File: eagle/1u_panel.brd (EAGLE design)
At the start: 83 x 100 mm, 61 parts, among them J1 1.27MM-SWD-CONNECTOR, U1 SPV1040, U5 P-CHANNELFET, U6 ON-N-CHANNEL-FET, U7 DIODE-INC-NPN

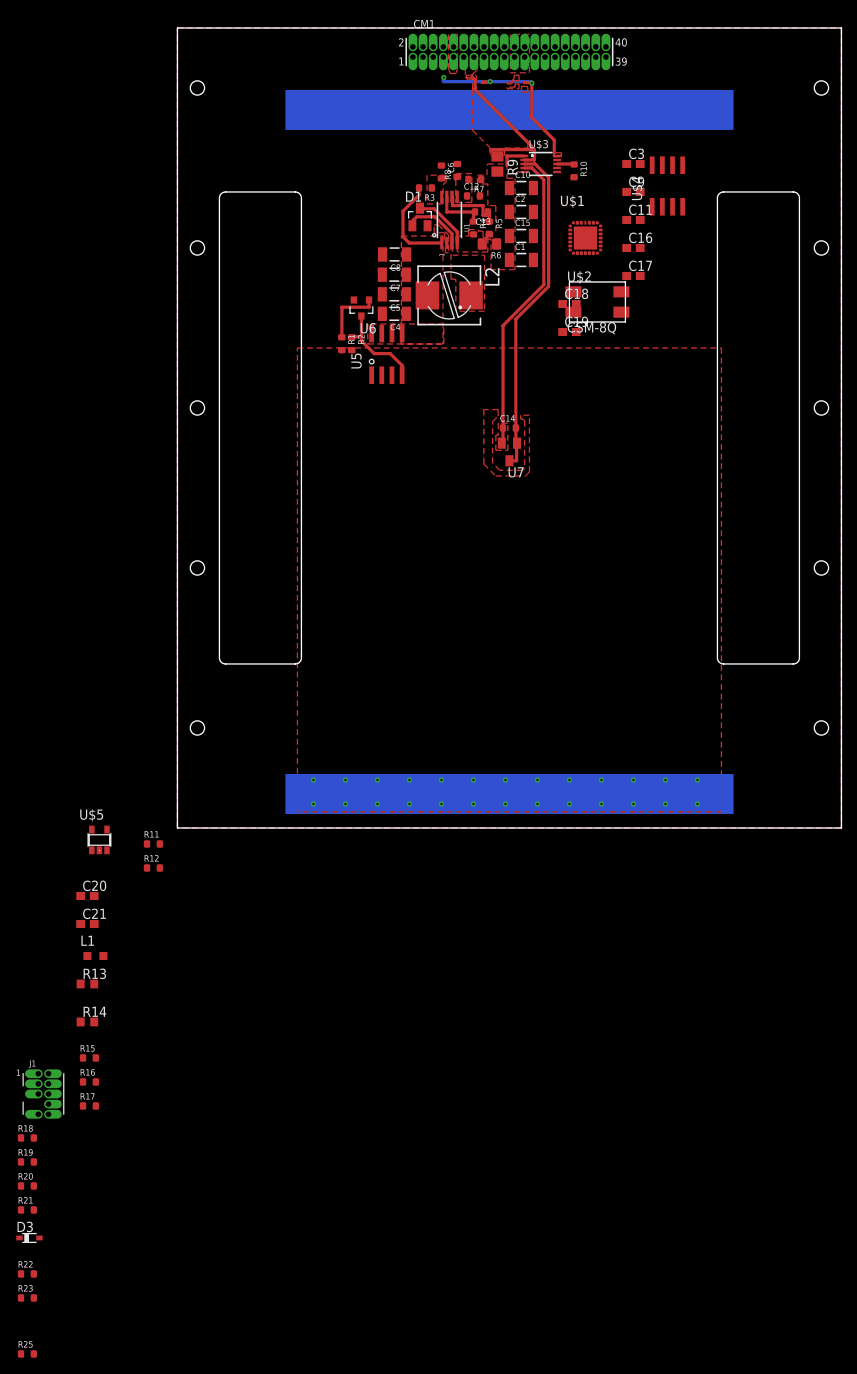
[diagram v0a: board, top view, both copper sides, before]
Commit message: Changed power output pins on header, placed components.
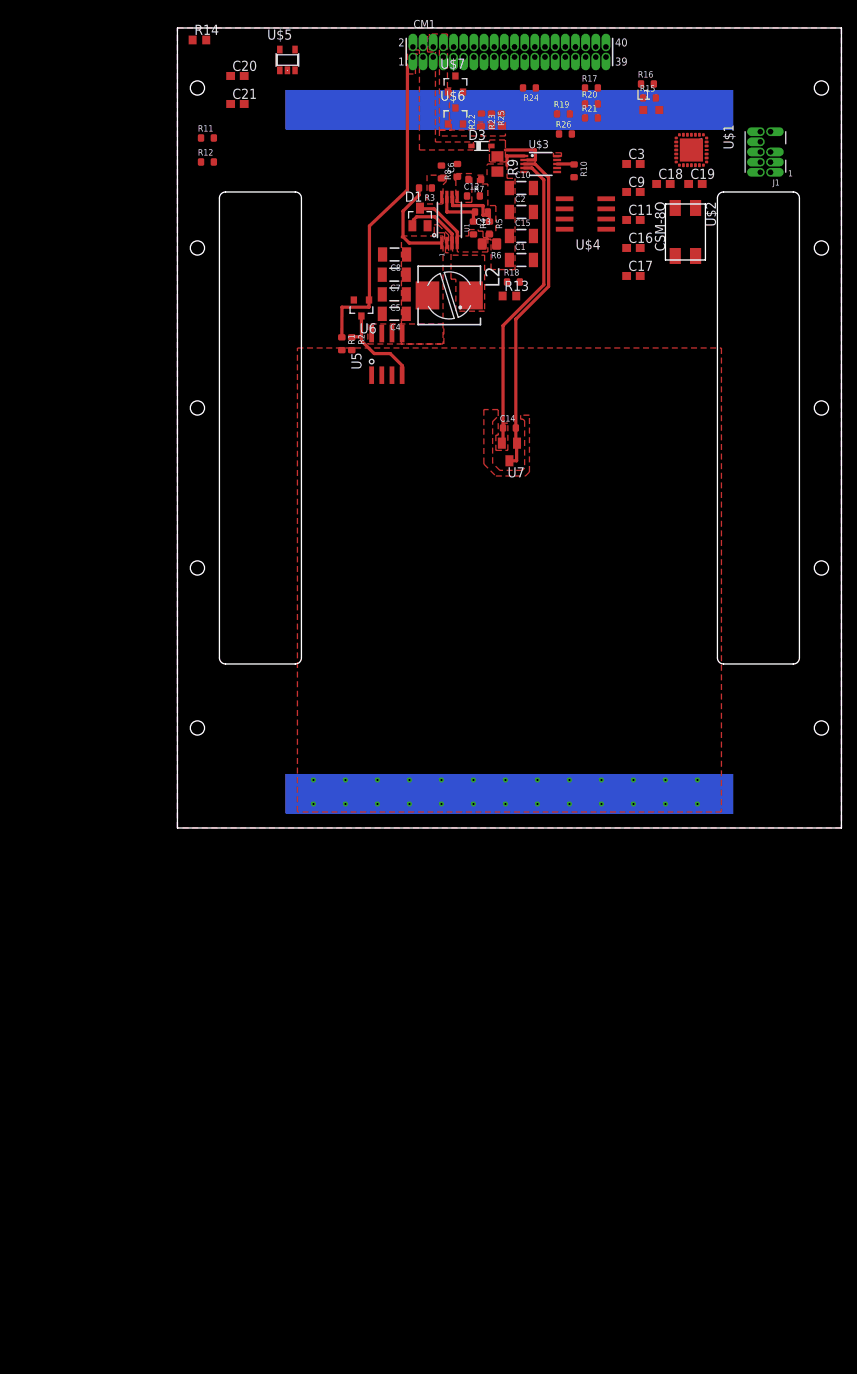
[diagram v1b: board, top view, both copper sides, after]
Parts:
- added R24, R26: NP, rcl_custom:.0603-B-NOSILK
- added U$6, U$7: ON-N-CHANNEL-FET, on-n-channel-fet:SOT23
- moved R25 164.8 mm to (39.2, 88.5), turned to 270 degrees
- moved R23 158.7 mm to (40.5, 88.5), turned to 90 degrees
- moved R22 155.0 mm to (38.0, 88.5), turned to 90 degrees
- moved R21 153.6 mm to (51.8, 88.8)
- moved R20 152.5 mm to (51.8, 90.5)
- moved J1 148.4 mm to (73.5, 84.5), turned to 180 degrees
- moved D3 147.7 mm to (38.0, 85.2)
- moved R19 147.1 mm to (48.2, 89.2)
- moved R16 142.9 mm to (58.8, 93.0)
- moved R17 141.9 mm to (51.8, 92.5)
- moved R15 138.9 mm to (59.0, 91.2)
- moved L1 126.5 mm to (59.2, 89.8)
- moved R14 123.5 mm to (2.75, 98.5)
- moved R18 123.0 mm to (42.0, 68.2)
- moved C20 104.2 mm to (7.50, 94.0)
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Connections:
- net ADDR0 renamed ADDRSELECT
- net N$13 renamed TDI
- net N$14 renamed SWO
- net N$16 renamed RESET
- net N$17 renamed SOLAR-IN-SWITCHED1
- net N$4 renamed SWDIO
- net N$5 renamed D
- net N$6 renamed R
- net N$9 renamed SWDCLK
- removed net N$10: U$4.7
- removed net N$12: U$4.6
- new net CANH: CM1.P$17, U$4.7
- new net CANL: CM1.P$19, U$4.6
- new net SCLOPT1ON: R24.2, U$6.2
- new net SCLOPT1OUT: CM1.P$14, U$6.3
- new net SDAOPT1ON: R26.2, U$7.2
- new net SDAOPT1OUT: CM1.P$12, U$7.3
- net GND: now also CM1.P$23, CM1.P$24, CM1.P$25, CM1.P$26
- net SCLOPT1: now also R24.1; no longer CM1.P$14
- net SDAOPT1: now also R26.1; no longer CM1.P$12
- net VCCOPT2: now also CM1.P$8, U$6.1, U$7.1
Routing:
- net SHORT: track 8.05 -> 39.3 mm
- net VCC: track 24.7 -> 0.00 mm, vias 3 -> 0
- net VSOLAR: track 20.3 -> 6.00 mm
- added copper zone on layer 1, net SOLAR-IN-SWITCHED1
- added copper zone on layer 1, net SWITCHEDOUT
- added copper zone on layer 1, net VCCOPT2
- removed copper zone on layer 1, net SOLAR-IN-SWITCHED2

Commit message: Board routing and fun times.
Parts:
- moved R14 65.0 mm to (57.0, 62.8)
- moved R11 64.1 mm to (65.0, 67.2), turned to 270 degrees
- moved C21 57.5 mm to (60.2, 67.5)
- moved C20 55.8 mm to (53.8, 62.8), turned to 180 degrees
- moved U$5 52.5 mm to (57.0, 66.2)
- moved R12 46.8 mm to (50.5, 83.5)
- moved C17 17.8 mm to (55.5, 86.8), turned to 180 degrees
- moved R20 12.8 mm to (39.0, 91.8)
- moved U$4 12.4 mm to (63.0, 73.8), turned to 180 degrees
- moved C9 10.4 mm to (55.5, 89.8), turned to 180 degrees
- moved R21 8.81 mm to (43.0, 87.8)
- moved U$2 8.28 mm to (55.2, 73.8)
- moved C16 8.08 mm to (54.0, 80.0), turned to 90 degrees
- moved R16 7.16 mm to (52.2, 90.0), turned to 180 degrees
- moved R24 7.04 mm to (37.2, 90.5)
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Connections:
- net N$8 renamed ADR1
- new net S$1: U$4.3
- new net S$2: U$1.1, U$1.5
- net 3.3V: no longer U$1.1, U$1.5, U$4.3
- net ADDRSELECT: no longer R10.1
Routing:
- net 3.3V: track 0.00 -> 34.6 mm, vias 0 -> 3
- net TDI: track 0.00 -> 13.2 mm, vias 0 -> 1
- net CRYSTALIN: track 0.00 -> 12.5 mm
- net CRYSTALOUT: track 0.00 -> 10.0 mm
- net SDAOPT1: track 0.00 -> 9.60 mm
- net SCLOPT1OUT: track 0.00 -> 8.68 mm
- net SCLOPT2: track 0.00 -> 8.16 mm
- net R: track 0.00 -> 7.87 mm, vias 0 -> 2
- net SWDIO: track 0.00 -> 7.31 mm
- net SWO: track 0.00 -> 6.81 mm
- net SWDCLK: track 0.00 -> 6.50 mm
- net VCCOPT1: track 0.00 -> 5.74 mm
- net SDAOPT1OUT: track 0.00 -> 4.77 mm
- net S$2: track 0.00 -> 4.35 mm
- net GND: track 0.00 -> 3.56 mm
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- added copper zone on layer 1, net 3.3V
- added copper zone on layer 16, net 3.3V
- added copper zone on layer 1, net CRYSTALIN
- added copper zone on layer 1, net D
- added copper zone on layer 1, net R
- added copper zone on layer 1, net SCLOPT1
- added copper zone on layer 1, net SCLOPT1ON
- added copper zone on layer 1, net SDAOPT1

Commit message: Fixed forward/back annotation errors. Yay.
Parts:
- moved R10 0.44 mm to (50.5, 82.2)
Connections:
- removed net S$1: U$4.3
- removed net S$2: U$1.1, U$1.5
- net 3.3V: now also U$1.1, U$1.5, U$4.3
- net ADDRSELECT: now also R10.1
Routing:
- net S$2: track 4.35 -> 0.00 mm
- net S$3: track 2.85 -> 0.00 mm
- net ADDRSELECT: track 2.81 -> 0.00 mm

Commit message: More routing fun times goody.
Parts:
- U7: value DIODE-INC-NPN -> DIODE-INC-NPNSOT23HOLE; device diodes-inc-npn:SOT23 -> diodes-inc-npn:SOT23HOLE
- moved C20 3.34 mm to (54.5, 66.0), turned to 90 degrees
- moved R18 2.46 mm to (39.8, 69.2), turned to 270 degrees
- moved R14 2.06 mm to (59.0, 63.2), turned to 180 degrees
- moved R13 1.77 mm to (39.8, 66.2), turned to 90 degrees
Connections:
- net CANH renamed RATS
- net N$11 renamed STEPD
- net N$15 renamed VDIV
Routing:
- net STEPD: track 0.00 -> 31.1 mm, vias 0 -> 2
- net CRYSTALOUT: track 10.0 -> 34.6 mm, vias 0 -> 2
- net VDIV: track 0.00 -> 22.3 mm, vias 0 -> 2
- net CRYSTALIN: track 12.5 -> 34.4 mm, vias 0 -> 2
- net 3.3V: track 34.6 -> 47.1 mm, vias 3 -> 4
- net GND: track 3.56 -> 15.3 mm
- net ADDRSELECT: track 0.00 -> 2.31 mm
- added copper zone on layer 1, net SOLAR-IN-SWITCHED2
- added copper zone on layer 16, net SOLAR-IN-SWITCHED2
- added copper zone on layer 1, net VDIV

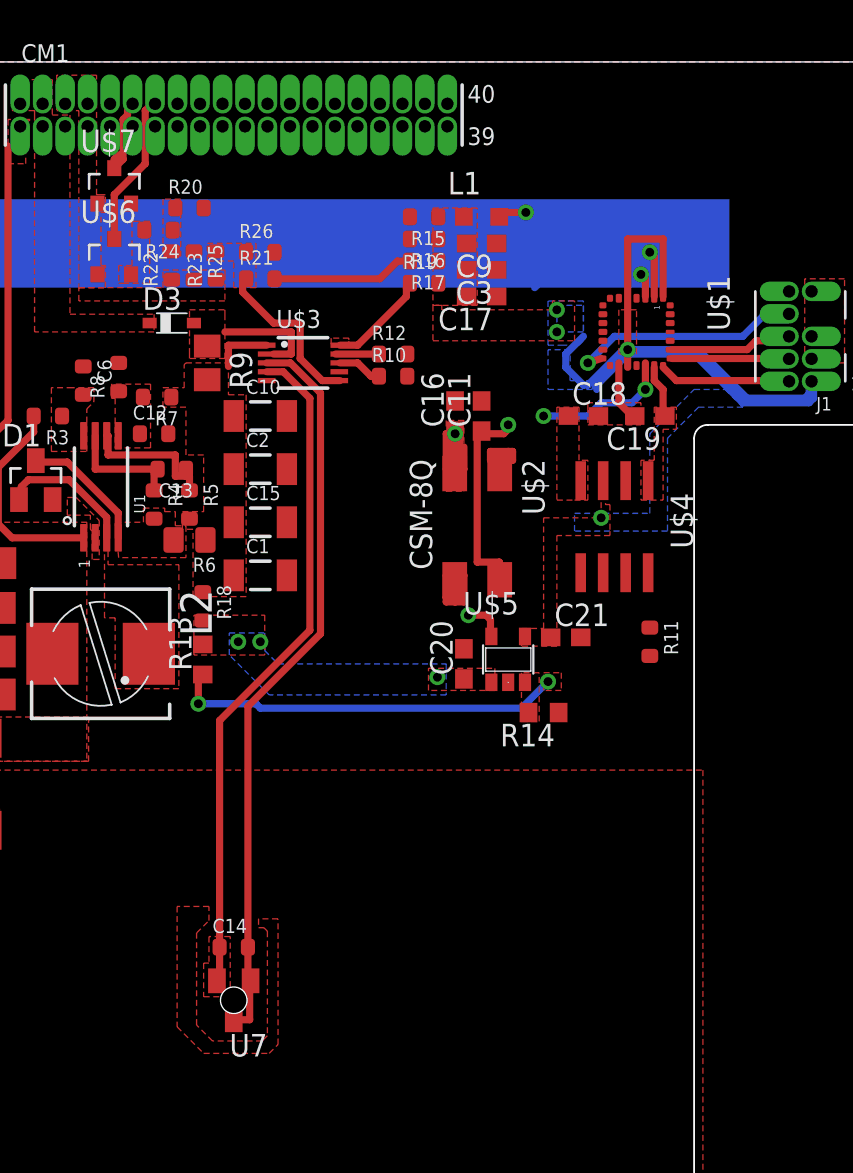
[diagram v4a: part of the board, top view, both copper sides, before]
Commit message: Finished board layout, fixed upside-down NPN pinout.
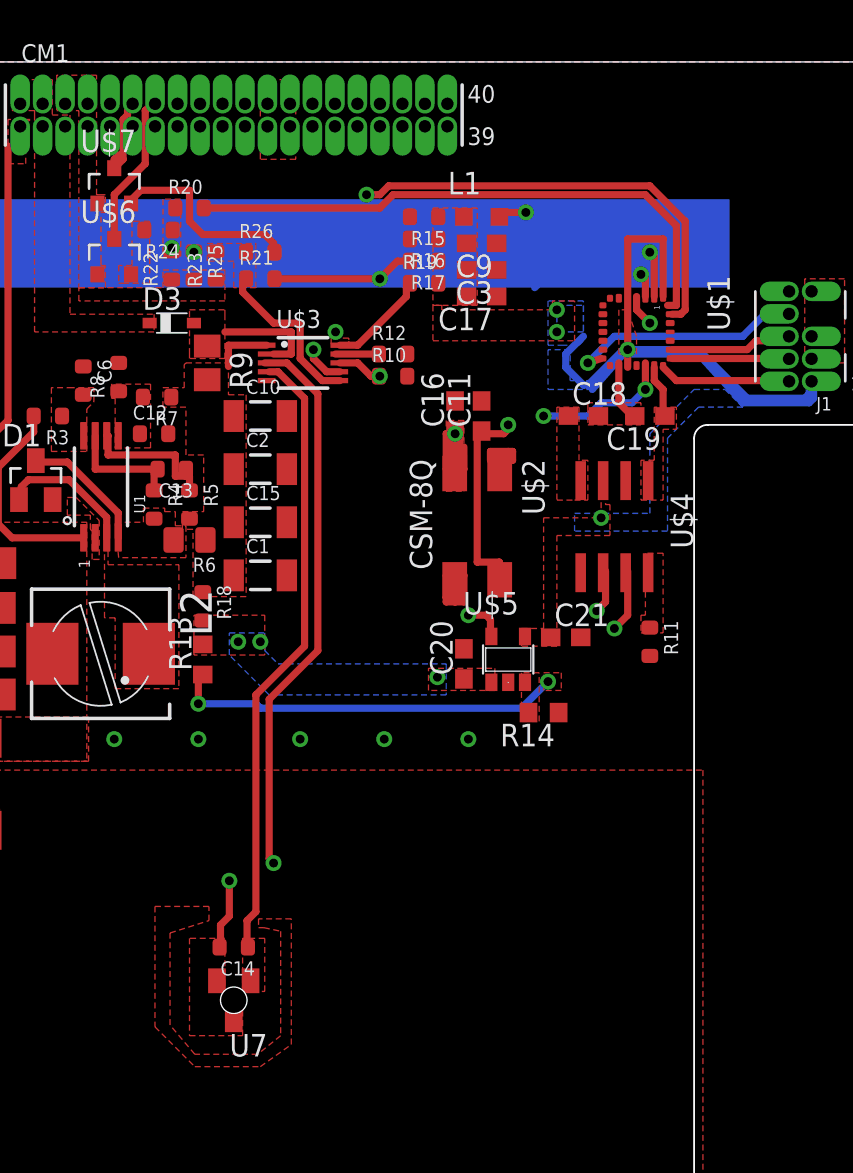
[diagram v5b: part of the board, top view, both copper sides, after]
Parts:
- turned C14 to 180 degrees
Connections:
- net N$2 renamed R11
- net RATS renamed CANH
- net ADDRSELECT: now also CM1.P$15
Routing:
- net CANH: track 0.00 -> 60.3 mm, vias 0 -> 1
- net CANL: track 0.00 -> 55.5 mm, vias 0 -> 1
- net SDAOPT2: track 0.00 -> 32.8 mm
- net SCLOPT2: track 8.16 -> 38.1 mm, vias 0 -> 2
- net ADDRSELECT: track 2.31 -> 23.5 mm, vias 0 -> 1
- net SCLOPT1: track 0.00 -> 15.5 mm, vias 0 -> 2
- net SDAOPT1ON: track 0.00 -> 11.1 mm
- net VCCOPT1: track 5.74 -> 16.6 mm, vias 0 -> 2
- net RESET: track 0.00 -> 10.3 mm, vias 0 -> 1
- net V3: track 41.8 -> 38.3 mm, vias 0 -> 2
- net V4: track 38.1 -> 35.0 mm
- net GND: vias 0 -> 5
- added copper zone on layer 15, net ADDRSELECT
- added copper zone on layer 15, net CANH
- added copper zone on layer 15, net CANL
- added copper zone on layer 15, net N$2
- added copper zone on layer 1, net R11
- added copper zone on layer 1, net V3
- added copper zone on layer 1, net VCCOPT1
- removed copper zone on layer 1, net VCC
